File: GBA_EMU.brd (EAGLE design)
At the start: 130.7 x 72.9 mm, 74 parts, among them J1 USB-MINIB-5PIN, J2 AVR_SPI, Q1 MOSFET-PCHANNEL, SW1 LEFT, SW2 RIGHT, SW3 PWR_SWITCH, U2 FT230X, U4 LM4875, U5 V_REG_LDOSMD2, U7 AZV321, X2 HEADPHONE

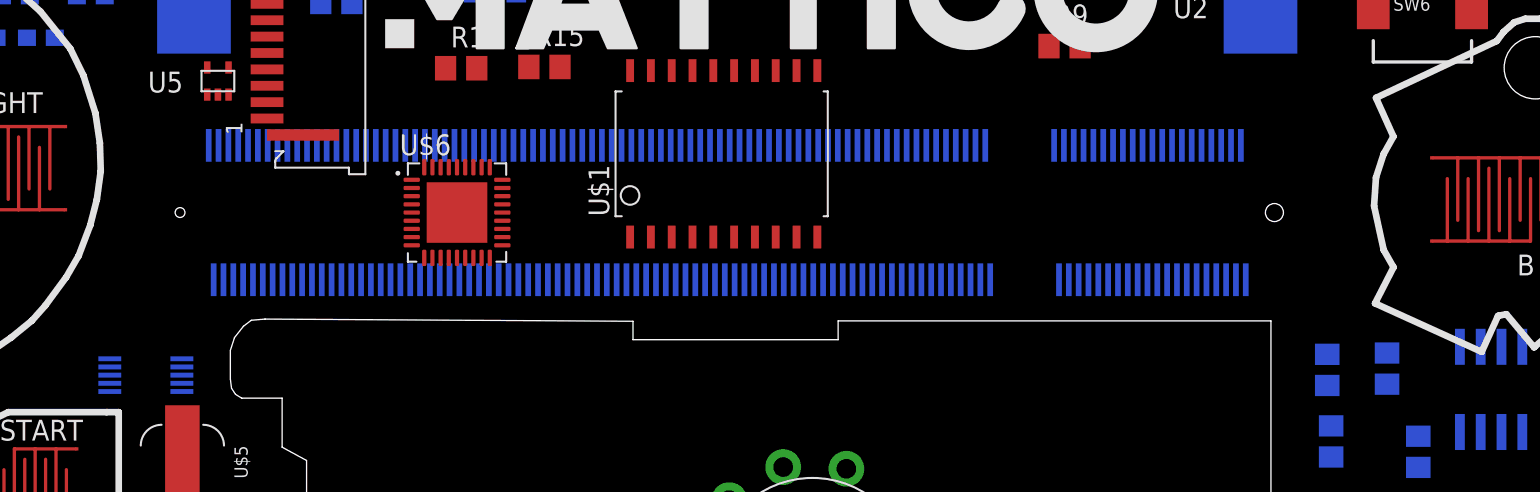
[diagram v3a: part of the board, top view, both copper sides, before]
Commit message: connected DAC directly to the Atmega
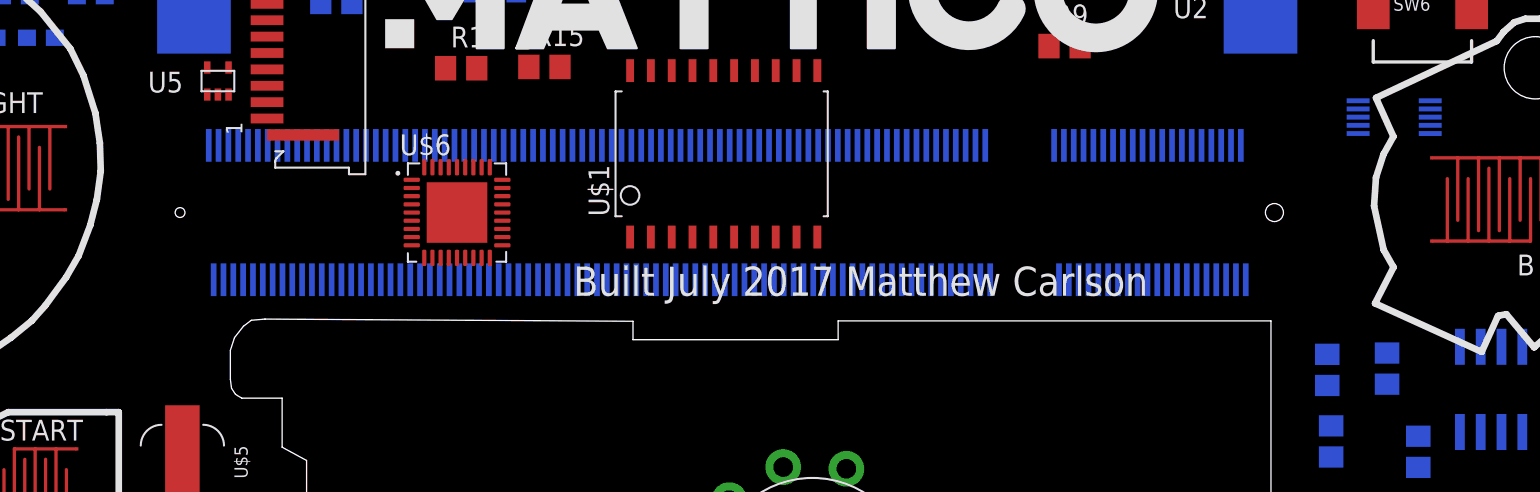
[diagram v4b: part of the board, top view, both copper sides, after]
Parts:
- moved U$3 77.8 mm to (126.8, 54.1)
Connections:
- removed net MISO: U$3.8
- net COPRO_MISO: now also U$3.8
- net COPRO_MOSI: now also U$3.10
- net COPRO_SCK: now also U$3.9
- net MOSI: no longer U$3.10
- net SCLK: no longer U$3.9
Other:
- board text added: "Built July 2017 Matthew Carlson"
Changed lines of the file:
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@@
 <hole x="25.69559375" y="37.732890625" drill="4"/>
 <wire x1="80.33825" y1="41.623790625" x2="57.87603125" y2="41.75745" width="0" layer="20"/>
+<text x="76.708" y="43.18" size="1.778" layer="21">Built July 2017 Matthew Carlson</text>
 </plain>
 <attributes>
@@
 <element name="R16" library="rcl" package="R0805" value="270R" x="137.16" y="27.94"/>
 <element name="U$2" library="custom" package="LOGO_2INCH_SVG" value="LOGO2INCH_SVG" x="64.572" y="57.524"/>
-<element name="U$3" library="custom" package="10-MSOP" value="MCP48FEB01-E/UN" x="50.6" y="38.336" rot="MR180"/>
+<element name="U$3" library="custom" package="10-MSOP" value="MCP48FEB01-E/UN" x="126.8" y="54.084" rot="MR180"/>
 <element name="U$1" library="custom" package="S020-75MM" value="CBT3244AD" x="80.16" y="51.844" rot="R90"/>
 <element name="POT1" library="adafruit" package="THUMBWHEEL" value="THUMBPOT" x="91.2908" y="26.0612" rot="R195"/>
@@
 <wire x1="58.34" y1="44.16" x2="60.14" y2="44.16" width="0" layer="19" extent="16-16"/>
 <wire x1="55.94" y1="44.16" x2="58.34" y2="44.16" width="0" layer="19" extent="16-16"/>
-<wire x1="84.29875" y1="74.850625" x2="80.264" y2="73.152" width="0" layer="19" extent="16-16"/>
-<wire x1="68.84" y1="52.36" x2="68.9" y2="57.07" width="0" layer="19" extent="1-16"/>
+<wire x1="69.596" y1="48.26" x2="69.14" y2="44.16" width="0" layer="19" extent="1-16"/>
+<wire x1="68.84" y1="52.36" x2="69.596" y2="48.26" width="0" layer="19" extent="1-16"/>
 <wire x1="70.64" y1="52.36" x2="68.84" y2="52.36" width="0" layer="19" extent="16-16"/>
 <wire x1="72.44" y1="52.36" x2="70.64" y2="52.36" width="0" layer="19" extent="16-16"/>
@@
 <wire x1="55.64" y1="52.36" x2="58.04" y2="52.36" width="0" layer="19" extent="16-16"/>
 <wire x1="55" y1="55.46125" x2="55.64" y2="52.36" width="0" layer="19" extent="1-16"/>
+<wire x1="84.29875" y1="74.850625" x2="80.264" y2="73.152" width="0" layer="19" extent="16-16"/>
 <wire x1="63.18" y1="61.11875" x2="58" y2="61" width="0" layer="19" extent="1-16"/>
 <wire x1="70.61365" y1="62.309375" x2="75.25" y2="64.77" width="0" layer="19" extent="1-16"/>
@@
 <wire x1="115.94" y1="44.16" x2="114.14" y2="44.16" width="0" layer="19" extent="16-16"/>
 <wire x1="117.74" y1="44.16" x2="115.94" y2="44.16" width="0" layer="19" extent="16-16"/>
-<wire x1="52.8" y1="38.836" x2="55.94" y2="44.16" width="0" layer="19" extent="16-16"/>
 <wire x1="122.71375" y1="39.605625" x2="117.74" y2="44.16" width="0" layer="19" extent="16-16"/>
 <wire x1="126.365" y1="39.685" x2="122.71375" y2="39.605625" width="0" layer="19" extent="16-16"/>
 <wire x1="122.951875" y1="35.24" x2="122.71375" y2="39.605625" width="0" layer="19" extent="16-16"/>
 <wire x1="132.08" y1="40.065" x2="126.365" y2="39.685" width="0" layer="19" extent="16-16"/>
+<wire x1="129" y1="54.584" x2="125.524" y2="60.452" width="0" layer="19" extent="1-16"/>
 <wire x1="91.125" y1="73.025" x2="84.29875" y2="74.850625" width="0" layer="19" extent="16-16"/>
 <wire x1="129.090321875" y1="46.519734375" x2="132.08" y2="40.065" width="0" layer="19" extent="1-16"/>
@@
 <wire x1="125.73" y1="27.625" x2="122.951875" y2="27.625" width="0" layer="19" extent="16-16"/>
 <wire x1="133.178471875" y1="27.330959375" x2="125.73" y2="27.625" width="0" layer="19" extent="16-16"/>
-<wire x1="46.387653125" y1="33.8340125" x2="52.8" y2="38.836" width="0" layer="19" extent="1-16"/>
-<wire x1="46.42191875" y1="25.943271875" x2="46.387653125" y2="33.8340125" width="0" layer="19" extent="1-1"/>
 <wire x1="46.394" y1="61.468" x2="48.462" y2="69.596" width="0" layer="19" extent="16-16"/>
 <wire x1="43.522" y1="61.468" x2="46.394" y2="61.468" width="0" layer="19" extent="16-16"/>
@@
 <wire x1="37.677790625" y1="45.56770625" x2="39.3446" y2="51.492" width="0" layer="19" extent="1-16"/>
 <wire x1="45.69403125" y1="53.50889375" x2="39.3446" y2="51.492" width="0" layer="19" extent="1-16"/>
+<wire x1="46.42191875" y1="25.943271875" x2="38.156" y2="23.384" width="0" layer="19" extent="1-1"/>
+<wire x1="46.387653125" y1="33.8340125" x2="46.42191875" y2="25.943271875" width="0" layer="19" extent="1-1"/>
 <wire x1="113.355" y1="63.165" x2="105.73" y2="58.42" width="0" layer="19" extent="1-1"/>
 <wire x1="112.705" y1="68.915" x2="113.355" y2="63.165" width="0" layer="19" extent="1-1"/>
 <wire x1="97.31125" y1="64.77" x2="91.125" y2="73.025" width="0" layer="19" extent="16-16"/>
 <wire x1="147" y1="28.575" x2="133.178471875" y2="27.330959375" width="0" layer="19" extent="16-16"/>
-<wire x1="69.596" y1="48.26" x2="38.156" y2="23.384" width="0" layer="19" extent="1-1"/>
 </signal>
 <signal name="TXD">
@@
 <contactref element="U$6" pad="29"/>
 <contactref element="U$6" pad="23"/>
-<wire x1="106.34" y1="44.16" x2="107.53" y2="67.31" width="0" layer="19" extent="1-16"/>
-<wire x1="57.14" y1="44.16" x2="106.34" y2="44.16" width="0" layer="19" extent="16-16"/>
-<wire x1="56.54" y1="44.16" x2="57.14" y2="44.16" width="0" layer="19" extent="16-16"/>
-<wire x1="56.84" y1="52.36" x2="57.14" y2="44.16" width="0" layer="19" extent="16-16"/>
-<wire x1="56.24" y1="52.36" x2="56.84" y2="52.36" width="0" layer="19" extent="16-16"/>
-<wire x1="48.4" y1="37.336" x2="56.54" y2="44.16" width="0" layer="19" extent="16-16"/>
-<wire x1="47.586" y1="64.516" x2="56.24" y2="52.36" width="0" layer="19" extent="16-16"/>
-<wire x1="71.096" y1="51.025" x2="48.4" y2="37.336" width="0" layer="19" extent="1-16"/>
-<wire x1="72.361" y1="48.26" x2="71.096" y2="51.025" width="0" layer="19" extent="1-1"/>
+<wire x1="106.34" y1="44.16" x2="124.6" y2="53.084" width="0" layer="19" extent="16-16"/>
+<wire x1="107.53" y1="67.31" x2="124.6" y2="53.084" width="0" layer="19" extent="1-16"/>
+<wire x1="72.361" y1="48.26" x2="106.34" y2="44.16" width="0" layer="19" extent="1-16"/>
+<wire x1="71.096" y1="51.025" x2="72.361" y2="48.26" width="0" layer="19" extent="1-1"/>
 <wire x1="67.596" y1="51.025" x2="71.096" y2="51.025" width="0" layer="19" extent="1-1"/>
 <wire x1="66.831" y1="48.26" x2="67.596" y2="51.025" width="0" layer="19" extent="1-1"/>
 <wire x1="67.596" y1="45.495" x2="66.831" y2="48.26" width="0" layer="19" extent="1-1"/>
 <wire x1="70.096" y1="45.495" x2="67.596" y2="45.495" width="0" layer="19" extent="1-1"/>
+<wire x1="57.14" y1="44.16" x2="66.831" y2="48.26" width="0" layer="19" extent="1-16"/>
+<wire x1="56.54" y1="44.16" x2="57.14" y2="44.16" width="0" layer="19" extent="16-16"/>
+<wire x1="56.84" y1="52.36" x2="57.14" y2="44.16" width="0" layer="19" extent="16-16"/>
+<wire x1="56.24" y1="52.36" x2="56.84" y2="52.36" width="0" layer="19" extent="16-16"/>
+<wire x1="47.586" y1="64.516" x2="56.24" y2="52.36" width="0" layer="19" extent="16-16"/>
 </signal>
 <signal name="1.8V">
@@
 <contactref element="R16" pad="1"/>
 <contactref element="U$3" pad="4"/>
-<wire x1="48.4" y1="38.836" x2="136.21" y2="27.94" width="0" layer="19" extent="1-16"/>
+<wire x1="136.21" y1="27.94" x2="124.6" y2="54.584" width="0" layer="19" extent="1-16"/>
 </signal>
 <signal name="N$18">
 </signal>
 <signal name="MOSI">
-<contactref element="U$3" pad="10"/>
 <contactref element="TFT1" pad="6"/>
-<wire x1="52.8" y1="37.336" x2="58" y2="59" width="0" layer="19" extent="1-16"/>
 </signal>
 <signal name="SCLK">
-<contactref element="U$3" pad="9"/>
 <contactref element="TFT1" pad="3"/>
-<wire x1="52.8" y1="37.836" x2="58" y2="56" width="0" layer="19" extent="1-16"/>
-</signal>
-<signal name="MISO">
-<contactref element="U$3" pad="8"/>
 </signal>
 <signal name="DAC_REF">
@@
 <contactref element="COPRO" pad="15"/>
 <contactref element="J2" pad="3"/>
+<contactref element="U$3" pad="9"/>
+<wire x1="77.724" y1="70.612" x2="129" y2="53.584" width="0" layer="19" extent="16-16"/>
 <wire x1="33.052" y1="45.9994" x2="77.724" y2="70.612" width="0" layer="19" extent="16-16"/>
 </signal>
@@
 <contactref element="COPRO" pad="16"/>
 <contactref element="J2" pad="4"/>
+<contactref element="U$3" pad="10"/>
+<wire x1="77.724" y1="73.152" x2="129" y2="53.084" width="0" layer="19" extent="16-16"/>
 <wire x1="32.252" y1="45.9994" x2="77.724" y2="73.152" width="0" layer="19" extent="16-16"/>
 </signal>
@@
 <contactref element="COPRO" pad="17"/>
 <contactref element="J2" pad="1"/>
+<contactref element="U$3" pad="8"/>
+<wire x1="75.184" y1="70.612" x2="129" y2="54.084" width="0" layer="19" extent="16-16"/>
 <wire x1="30.7594" y1="47.492" x2="75.184" y2="70.612" width="0" layer="19" extent="16-16"/>
 </signal>

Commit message: moved some parts arounf
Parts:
- moved U$6 16.3 mm to (53.3, 47.2)
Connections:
- new net JOY_BTN: U$4.P$7
- net 3.3V: now also U$4.P$1, U$4.P$4
- net DOWN: now also COPRO.7
- net JOY_H: no longer U$4.P$1, U$4.P$4
- net LEFT: now also COPRO.8
- net RIGHT: now also COPRO.9
- net UP: now also COPRO.6
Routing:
- added copper zone on layer 16, net GND

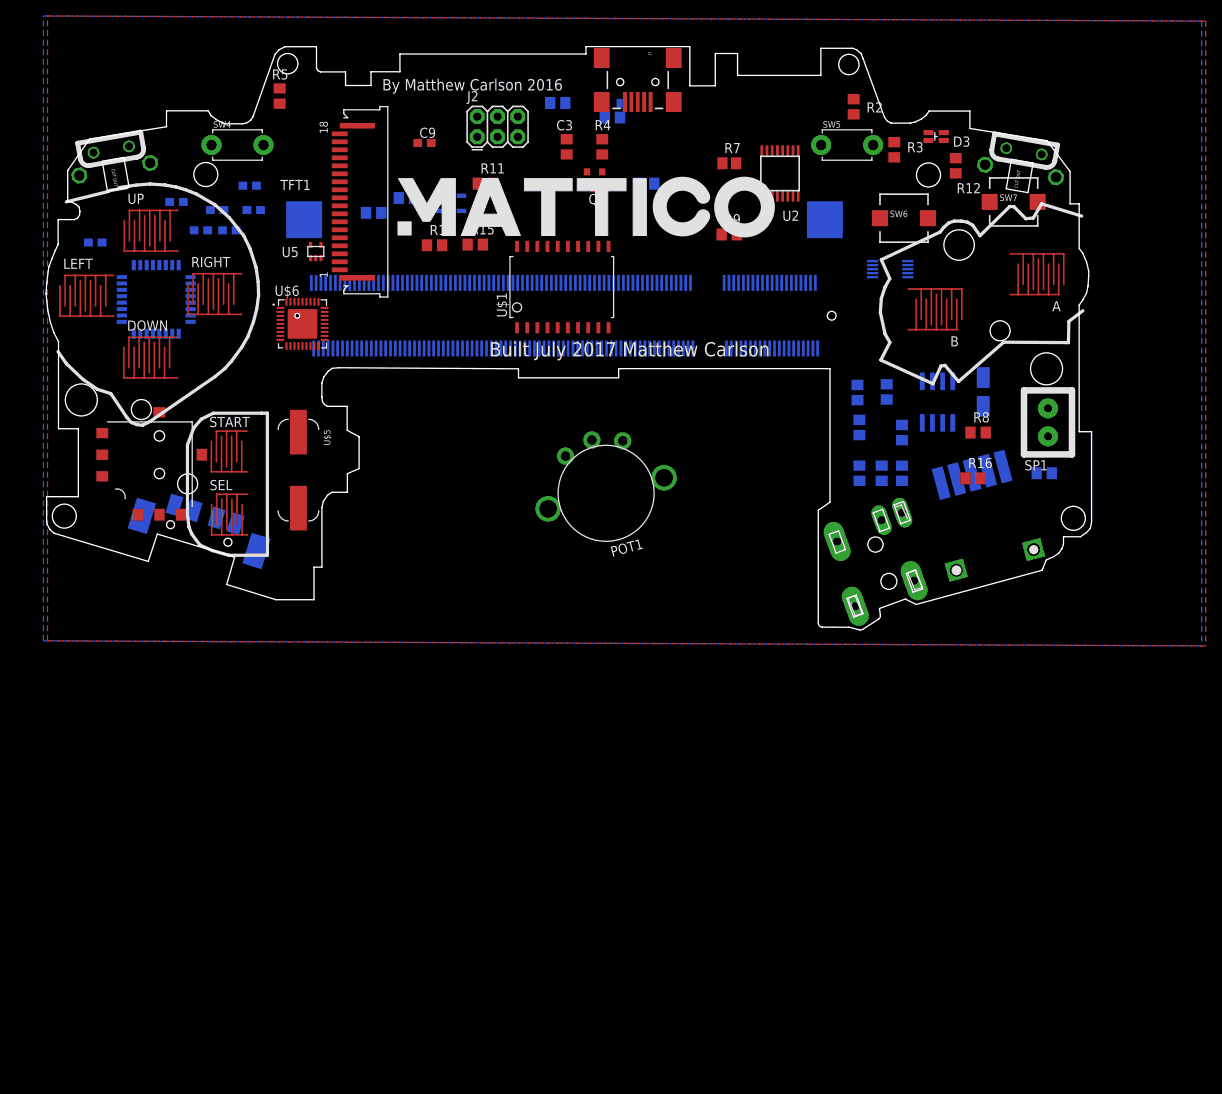
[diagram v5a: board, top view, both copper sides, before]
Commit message: added a uSD card slot and a few test points
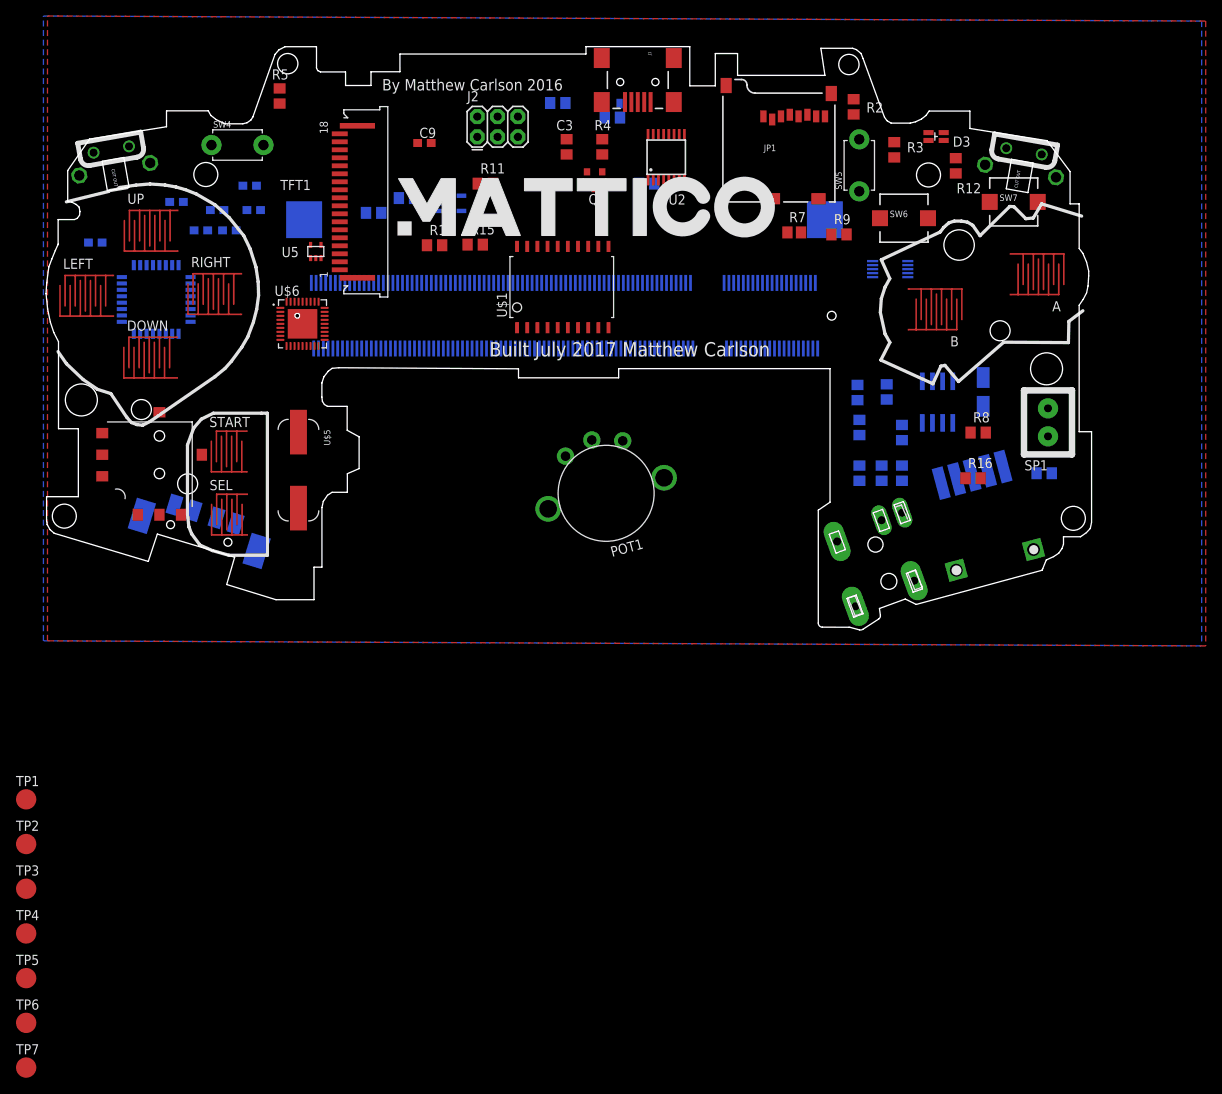
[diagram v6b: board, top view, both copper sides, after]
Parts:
- added JP1: USD-SOCKETNEW, SparkFun-Connectors:MICRO-SD-SOCKET-PP
- added TP1, TP2, TP3, TP4, TP5, TP6, TP7: TPB2,54, testpad:B2,54
- moved U2 14.4 mm to (98.8, 68.1)
- moved R9 13.7 mm to (120.4, 58.4)
- moved R7 11.9 mm to (114.8, 58.7)
- moved SW5 2.96 mm to (122.9, 67.1), turned to 90 degrees
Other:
- outline, holes or cut-outs redrawn
